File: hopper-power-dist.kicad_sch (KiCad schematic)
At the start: 27 parts, among them J1 XT60PW-M, J2 XT60PW-M, J3 B2B-XH-A(LF)(SN), J4 B2B-XH-A(LF)(SN), J5 XT60-F, J6 XT60PW-F, J7 XT60PW-F, J8 XT60PW-F, J9 XT60PW-F, SW1 FT_Power_Switch

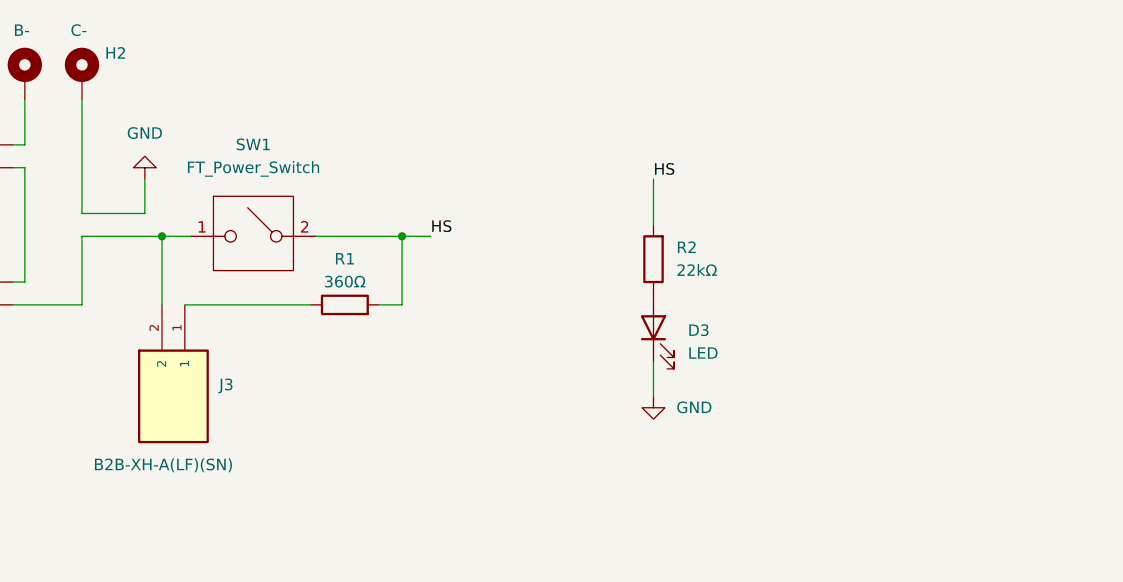
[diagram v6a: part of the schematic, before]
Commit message: Added spark suppression and changed thermal reliefs to solid on high power pads
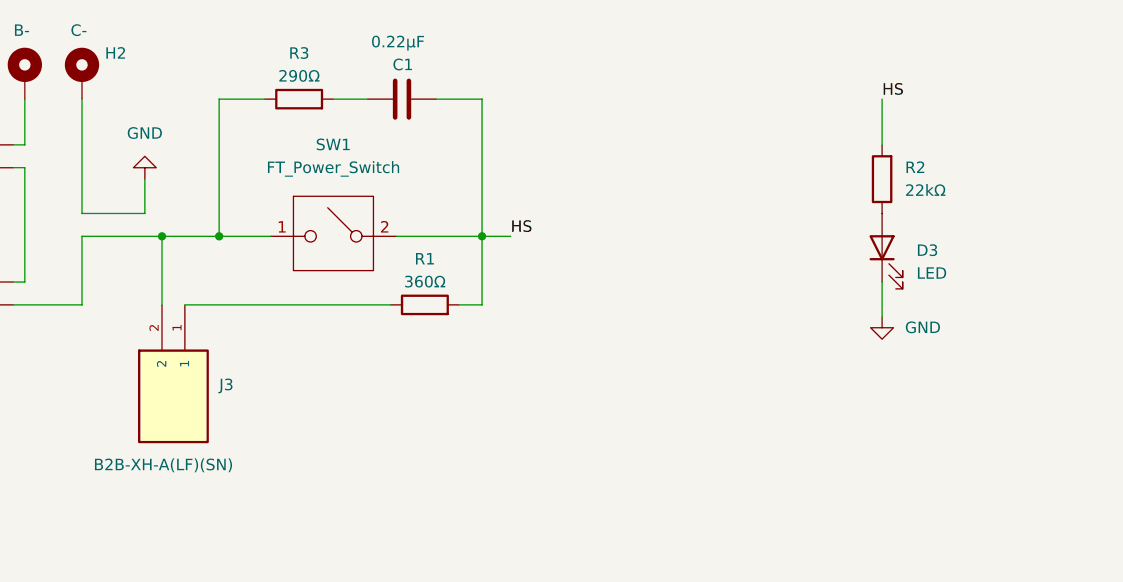
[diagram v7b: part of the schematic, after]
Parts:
- added C1: 0.22μF, Capacitor_SMD:C_1206_3216Metric, symbol Device:C
- added R3: 290Ω, Resistor_SMD:R_2512_6332Metric, symbol Device:R
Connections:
- net HS: now also C1.2
- net at J2.1 (+), J3.2, SW1.1: now also R3.1
- new net: C1.1, R3.2
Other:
- moved on the sheet: D3, R1, R2, SW1

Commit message: Started rev03 design
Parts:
- removed C1: 0.22μF, Capacitor_SMD:C_1206_3216Metric, symbol Device:C
- removed C2: 4.7μF, SamacSys_Parts:CAPC3225X270N, symbol Device:C
- removed C3: 4.7μF, Capacitor_SMD:C_0805_2012Metric, symbol Device:C
- removed C4, C5: 1000pF, Capacitor_SMD:C_1206_3216Metric, symbol Device:C
- removed C6: 470pF, Capacitor_SMD:C_1206_3216Metric, symbol Device:C
- removed D1: AK3-066C-Y, SamacSys_Parts:AK3066CY, symbol AK3-066C-Y:AK3-066C-Y
- removed D2: SMDJ17A, DIOM7959X262N, symbol SamacSys_Parts:SMDJ17A
- removed J3, J4: B2B-XH-A(LF)(SN), JST_B2B-XH-A(LF)(SN), symbol B2B-XH-A_LF__SN_:B2B-XH-A(LF)(SN)
- removed L1, L2: 12μF, SamacSys_Parts:LPS6235123MRC, symbol Device:L
- removed PS1: JTL6048S15, JTL6048S15, symbol SamacSys_Parts:JTL6048S15
- removed R1: 360Ω, benbokser:AC03000003600JAC00, symbol Device:R
- removed R3: 290Ω, Resistor_SMD:R_2512_6332Metric, symbol Device:R
- removed S1: 2MS6T1B3M2QES, 2MS6T1B3M2QES, symbol benbokser:2MS6T1B3M2QES
- removed SW1: FT_Power_Switch, benbokser:FT Power Switch, symbol benbokser:FT_Power_Switch
- added C?: 10nF, symbol Device:C
- added C?: 1μF, symbol Device:C
- added C?: 150μF, symbol Device:C_Polarized
- added C?: 47μF, symbol Device:C_Polarized
- added C?: 0.68μF, symbol Device:C
- added C?: 0.1μF, symbol Device:C
- added D?: SMBJ60A-E3_52, DIOM5436X244N, symbol SamacSys_Parts:SMBJ60A-E3_52
- added D?: 5.0SMDJ54CA-QH, DIONM7959X262N, symbol SamacSys_Parts:5.0SMDJ54CA-QH
- added D?: SMF24VTR, SMF24VTR, symbol SamacSys_Parts:SMF24VTR
- added J?: XT60-F, XT60PW-F:AMASS_XT60-F, symbol XT60PW-F:XT60-F
- added PS?: CQB100W14-72S24_, symbol custom-symbols:CQB100W14-72S24_
- added Q? (x3): PSMN3R9-100YSFX, symbol custom-symbols:PSMN3R9-100YSFX
- added R?: 1kΩ, Resistor_SMD:R_0603_1608Metric_Pad0.98x0.95mm_HandSolder, symbol Device:R
- added R?: 59kΩ, Resistor_SMD:R_0603_1608Metric_Pad0.98x0.95mm_HandSolder, symbol Device:R
- added R?: 24kΩ, Resistor_SMD:R_0603_1608Metric_Pad0.98x0.95mm_HandSolder, symbol Device:R
- added R?: 10Ω, Resistor_SMD:R_0603_1608Metric_Pad0.98x0.95mm_HandSolder, symbol Device:R
- added R?: 3.57kΩ, Resistor_SMD:R_0603_1608Metric_Pad0.98x0.95mm_HandSolder, symbol Device:R
- added R? (x2): 0.025Ω, Resistor_SMD:R_0603_1608Metric_Pad0.98x0.95mm_HandSolder, symbol Device:R
- added S? (x2): 2MS6T1B3M2QES, 2MS6T1B3M2QES, symbol 2ms6t1b3m2qes:2MS6T1B3M2QES
- added U?: MAX5933AESA, symbol custom-symbols:MAX5933AESA
- added Z?: SZMMBZ5264BLT1G, SOT96P237X111-3N, symbol SamacSys_Parts:SZMMBZ5264BLT1G
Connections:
- net GND: now also C?.2, C?.2, C?.2, C?.2, C?.2, C?.2, D?.2, D?.2, PS?.3 (-VIN), R?.1, U?.4 (GND)
- net HS: now also C?.1, D?.1, Q?.2 (S), Q?.2 (S), Q?.2 (S), R?.2, R?.2, Z?.1 (ANODE)
- net at J2.1 (+): now also C?.1, D?.1, R?.2, S?.3, U?.8 (VCC)
- net at F1.2: now also C?.1, C?.1, PS?.1 (+VIN)
- new net: C?.1, R?.1
- new net: R?.1, R?.2, U?.6 (GATE), Z?.3 (CATHODE)
- new net: R?.2, S?.1
- new net: Q?.1 (D), Q?.1 (D), Q?.1 (D), R?.1, U?.7 (SENSE)
- new net: Q?.3 (G), Q?.3 (G), Q?.3 (G), R?.2
- new net: R?.1, R?.2, U?.2 (FB)
- new net: R?.1, U?.1 (ON)
- new net: R?.1, U?.3 (PWRGOOD)
- new net: C?.1, U?.5 (TIMER)
- new net +24V: D?.1, J?.1 (+), PS?.8 (+VOUT)
- new net -24V: D?.2, J?.2 (-), PS?.4 (-VOUT)
- new net PS_EN: PS?.2 (EN)
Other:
- moved on the sheet: D3, F1, H1, H2, J1, J2, J5, J6, J7, J8, J9, R2
